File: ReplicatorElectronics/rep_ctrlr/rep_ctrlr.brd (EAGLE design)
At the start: 106.5 x 89 mm, 98 parts, among them IC1 MICROCHIP_PIC32MX7X5F256L-PF, IC2 MICROCHIP_MCP6001-LT, IC3 MICROCHIP_MCP6001-LT, IC4 MICROCHIP_MCP6001-LT, IC5 MICROCHIP_MCP6001-LT, J1 ATX24RH, J10 SBH11-PBPC-D07-ST-BK, J11 SBH11-PBPC-D07-ST-BK, J12 SBH11-PBPC-D07-ST-BK, J13 SBH11-PBPC-D07-ST-BK, J14 SBH11-PBPC-D07-ST-BK, J15 SBH11-PBPC-D07-ST-BK, J16 SBH11-PBPC-D07-ST-BK, J17 SBH11-PBPC-D07-ST-BK, J18 SI-50170-F, J19 70553-0106, J4 RJ11-2L-B, J6 SBH11-PBPC-D05-ST-BK, J7 SBH11-PBPC-D05-ST-BK, J8 SBH11-PBPC-D05-ST-BK, J9 SBH11-PBPC-D05-ST-BK, Q1 ASFL1, Q2 ASFL1, U18 LDS3985XX33

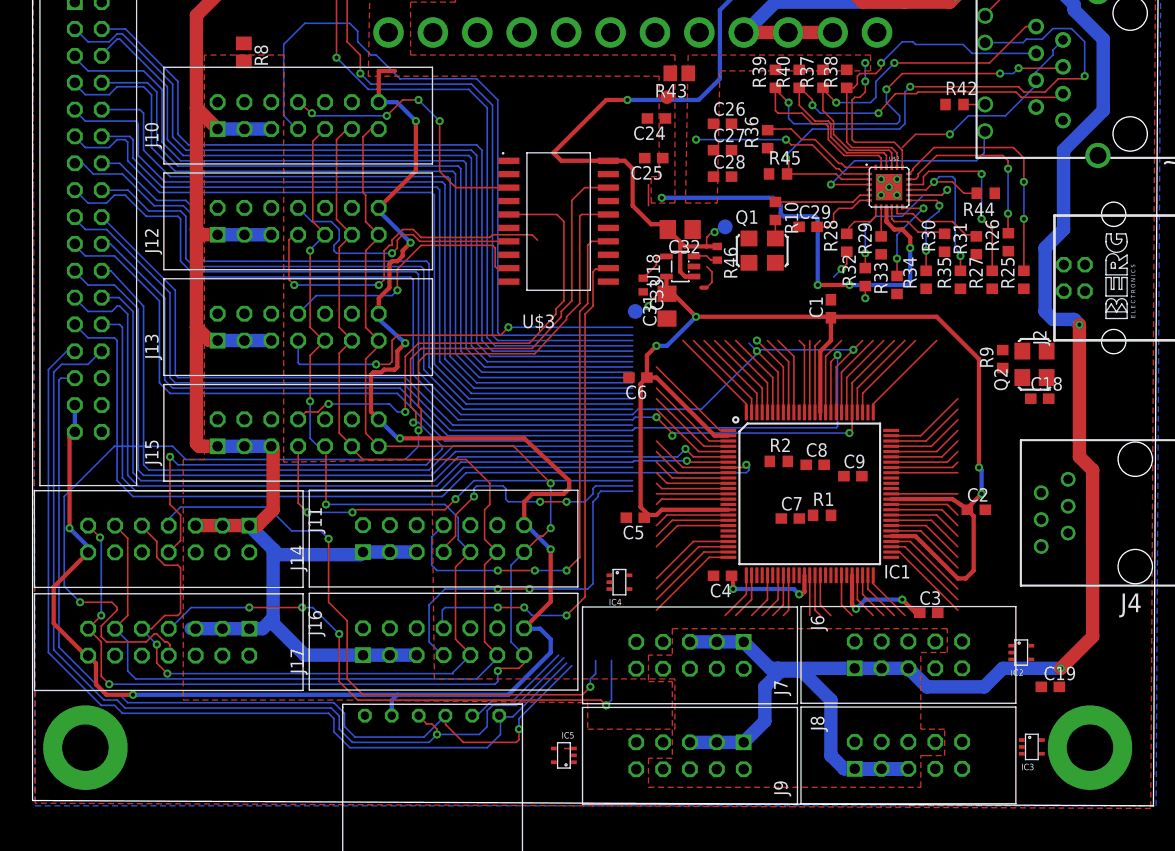
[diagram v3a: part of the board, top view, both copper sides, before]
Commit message: 5/16/12: All but PHY-PIC signals, encoder SPI bus (PIC pins only), servo signals (3.3V side only), and temperature inputs routed.
~ 4 hrs.
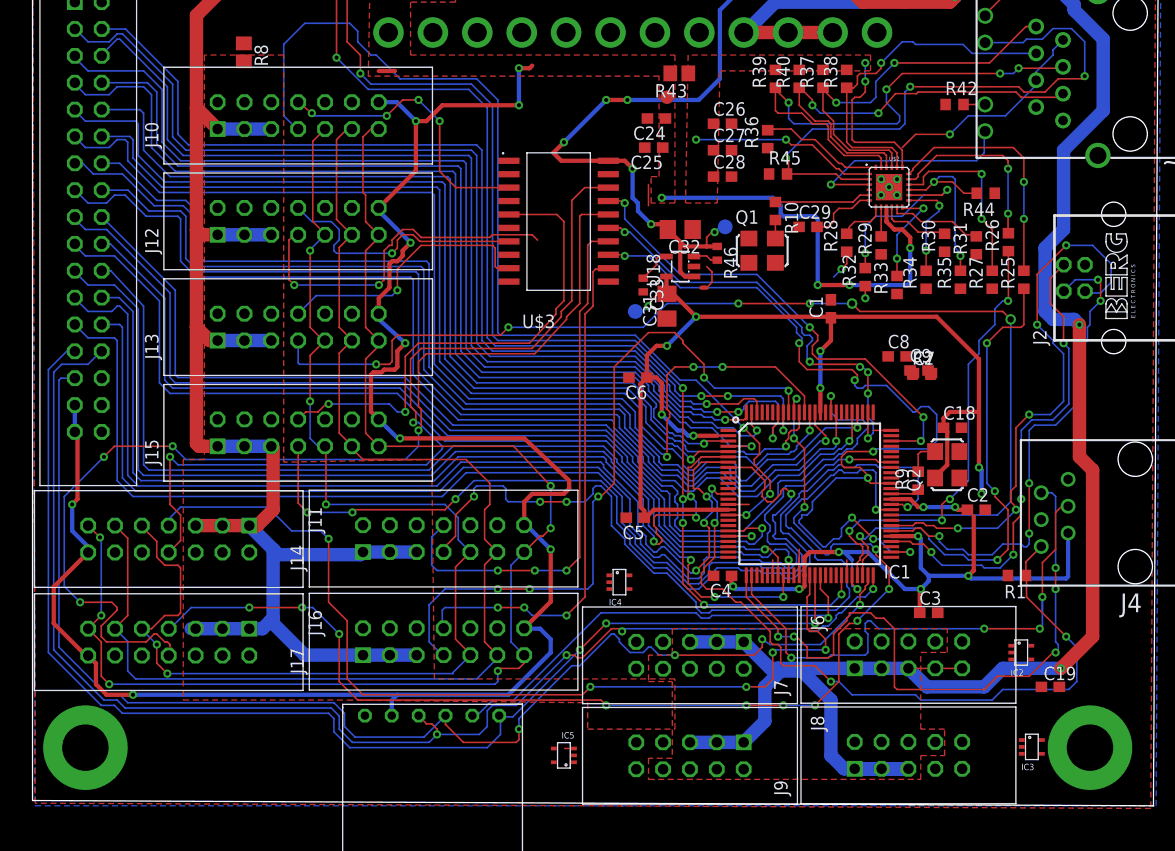
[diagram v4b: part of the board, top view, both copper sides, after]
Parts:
- moved R1 19.3 mm to (93.1, 21.8), turned to 180 degrees
- moved C7 18.6 mm to (84.2, 40.9)
- moved R2 15.8 mm to (84.1, 40.8)
- moved R9 14.0 mm to (83.8, 30.8)
- moved C8 12.9 mm to (81.8, 42.5)
- moved Q2 12.6 mm to (86.5, 32.2)
- moved C9 11.8 mm to (83.8, 41.2)
- moved C18 8.70 mm to (87.0, 35.8)
- moved C25 1.00 mm to (58.8, 62.2)
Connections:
- net DB17: now also U$1.18; no longer U$1.17
- net ENC_3_3V: now also C19.1, Q1.4, R14.2, R15.2, R17.2, R18.2, R20.2, R21.2, R23.2, R24.2
- net VCC: no longer C19.1, Q1.4, R14.2, R15.2, R17.2, R18.2, R20.2, R21.2, R23.2, R24.2
- net X+: now also U$1.17; no longer U$1.18
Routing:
- net SERVO2: track 8.58 -> 82.0 mm, vias 0 -> 8
- net MCLRN: track 6.80 -> 69.2 mm, vias 0 -> 4
- net ENC3_CSN: track 43.6 -> 102.8 mm, vias 2 -> 6
- net PGEC: track 4.63 -> 62.0 mm, vias 0 -> 5
- net ENC6_CSN: track 60.5 -> 110.9 mm, vias 4 -> 13
- net ENC4_CSN: track 31.3 -> 79.9 mm, vias 3 -> 4
- net PGED: track 4.42 -> 51.1 mm, vias 0 -> 4
- net USB_D+: track 7.54 -> 53.1 mm, vias 0 -> 5
- net ENC5_CSN: track 45.3 -> 90.7 mm, vias 3 -> 4
- net ETXD1: track 4.63 -> 48.5 mm, vias 0 -> 4
- net SERVO5: track 0.12 -> 41.6 mm, vias 0 -> 6
- net USB_D-: track 7.75 -> 47.8 mm, vias 0 -> 5
- net A0: track 89.0 -> 128.0 mm, vias 2 -> 7
- net SD_CSN: track 72.7 -> 111.7 mm, vias 0 -> 1
- net SERVO0: track 7.54 -> 46.0 mm, vias 0 -> 4
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
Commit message: 5/19/12: 18 PIC connections left. Ground currently fractured.
~3 hrs spent between last commit and this one.
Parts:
- C10, C11, C12, C13, C14, C15, C16, C17, C18, C7, C8, C9: device resistor:C0603 -> resistor:C0402
- C19, C30: device rcl:C0603 -> resistor:C0402
- R1, R10, R13, R14, R15, R16, R17, R18, R19, R2, R20, R21, R22, R23, R24, R9: device resistor:R0603 -> resistor:R0402
- moved C10 210.2 mm to (88.5, 19.9)
- moved R22 172.2 mm to (48.1, 3.22)
- moved R15 171.7 mm to (93.8, 18.7), turned to 90 degrees
- moved R14 171.4 mm to (95.0, 13.2)
- moved R13 168.7 mm to (94.3, 9.59), turned to 90 degrees
- moved C19 43.9 mm to (53.2, 20.2), turned to 90 degrees
- moved C8 4.83 mm to (86.3, 40.8)
- moved C5 4.81 mm to (54.8, 23.0)
- moved C9 4.26 mm to (86.6, 37.9)
- moved C7 3.20 mm to (86.7, 38.9)
- moved R2 3.01 mm to (86.3, 38.8)
- moved 3.3V 1.52 mm to (57.2, 48.2)
- moved IC4 1.30 mm to (56.1, 20.0), turned to 0 degrees
- moved IC2 1.25 mm to (94.5, 15.2)
- moved Q1 0.50 mm to (69.0, 53.0)
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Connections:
- net A0: now also U$1.24; no longer U$1.1
- net DB1: now also U$1.4; no longer U$1.3
- net DB2: now also U$1.3; no longer U$1.4
- net LCD_WR: now also U$1.1; no longer U$1.24
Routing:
- net ENC2_CSN: track 33.2 -> 166.0 mm, vias 2 -> 16
- net PS_ON: track 2.00 -> 79.1 mm, vias 0 -> 9
- net ERXD0: track 0.00 -> 69.9 mm, vias 0 -> 8
- net ERXD1: track 2.92 -> 72.5 mm, vias 1 -> 8
- net NRST: track 0.00 -> 59.6 mm, vias 0 -> 4
- net ECRSDV: track 0.00 -> 52.3 mm, vias 0 -> 2
- net SERVO7: track 0.00 -> 49.0 mm, vias 0 -> 4
- net EREFCLK: track 1.15 -> 49.7 mm, vias 1 -> 6
- net ERXERR: track 0.00 -> 48.0 mm, vias 0 -> 6
- net A0: track 128.0 -> 99.8 mm, vias 7 -> 5
- net ETXEN: track 0.00 -> 25.3 mm, vias 0 -> 2
- net EMDC: track 0.00 -> 24.7 mm, vias 0 -> 6
- net ETXD0: track 42.7 -> 66.8 mm, vias 4 -> 10
- net EMDIO: track 0.00 -> 24.0 mm, vias 0 -> 4
- net +3V3: track 169.5 -> 191.0 mm, vias 18 -> 27
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
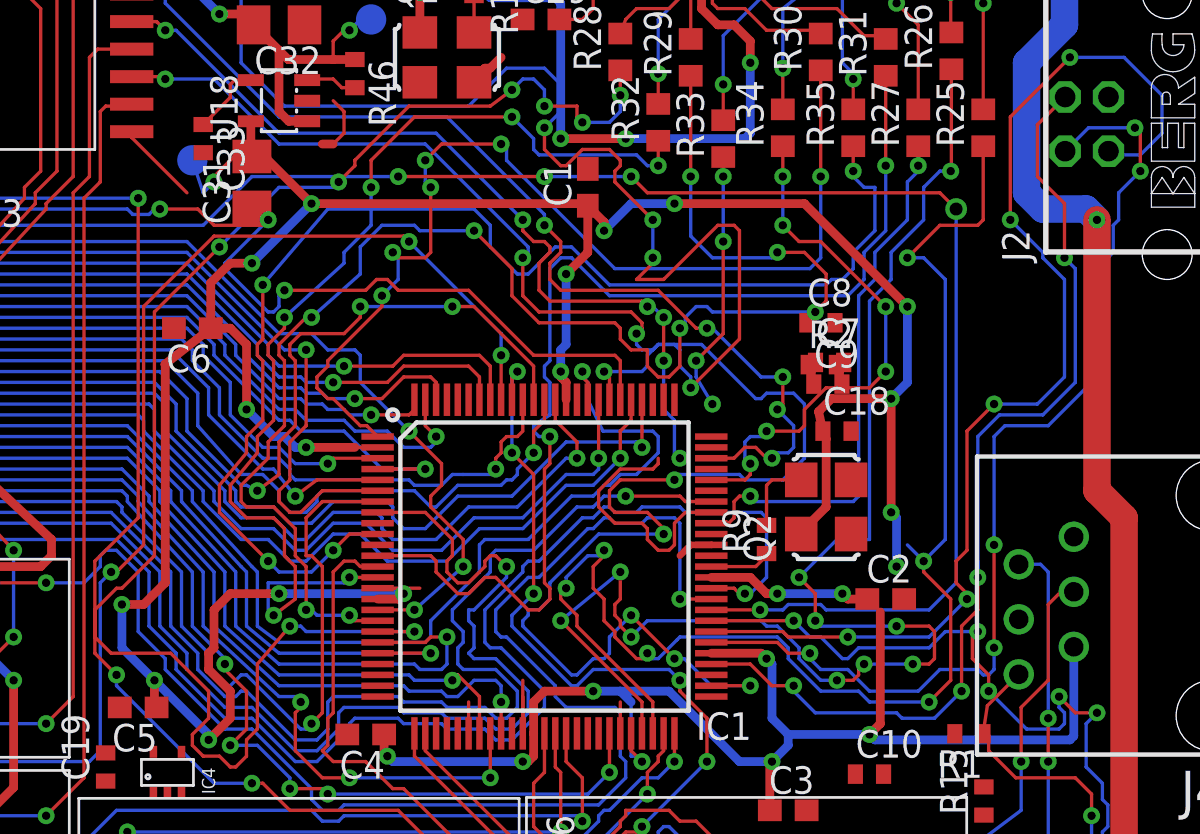
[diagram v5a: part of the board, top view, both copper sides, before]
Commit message: 5/21/12: Fixed GND plane. Still 18 PIC connections remaining...
~ 1 hr.
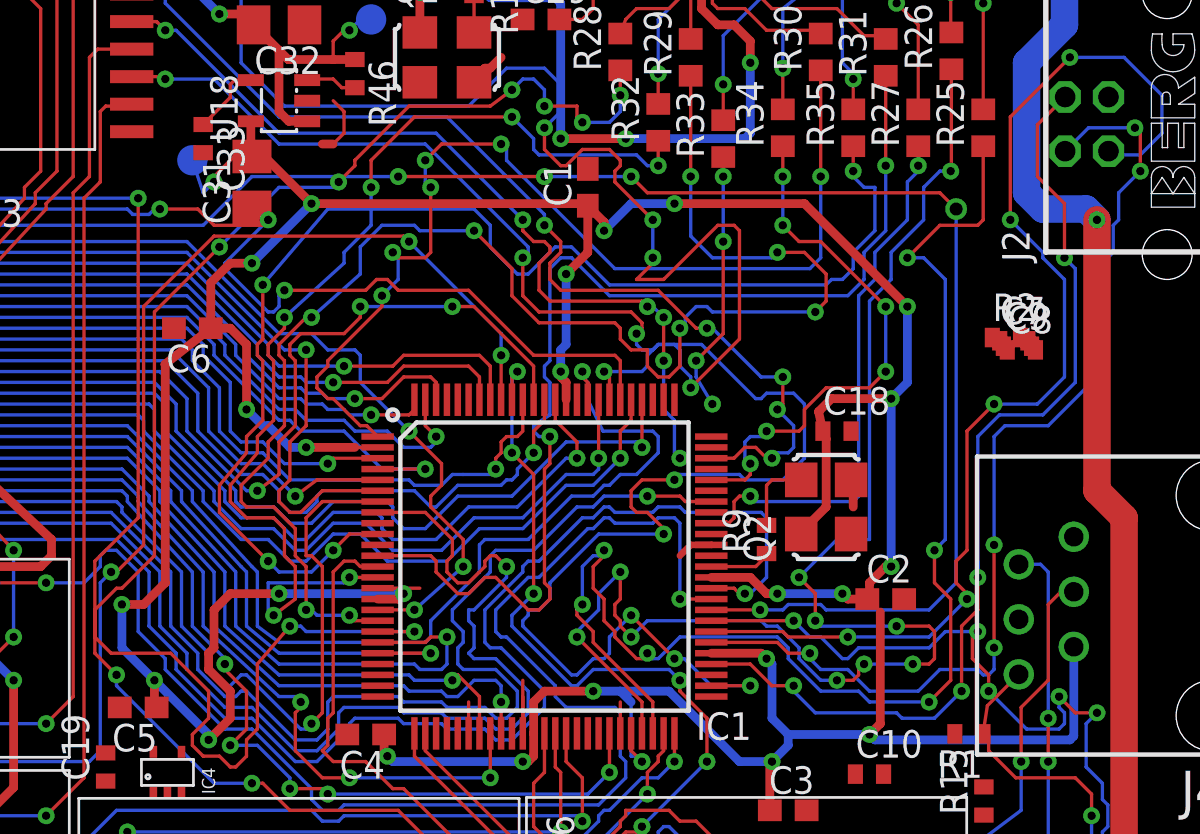
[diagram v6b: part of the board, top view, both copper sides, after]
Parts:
- moved C8 9.33 mm to (95.5, 39.5)
- moved C9 8.92 mm to (95.3, 39.7)
- moved R2 8.59 mm to (94.8, 40.1)
- moved C7 8.56 mm to (95.2, 39.9)
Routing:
- net EMDIO: track 24.0 -> 12.1 mm
- net SERVO3: track 3.88 -> 0.00 mm
- net ETXD1: track 64.7 -> 62.5 mm
- net SERVO2: track 81.7 -> 79.7 mm
- net +3V3: track 191.0 -> 193.0 mm, vias 27 -> 26
- net DGND: track 16.4 -> 17.7 mm
- net ETXD0: track 66.8 -> 66.0 mm

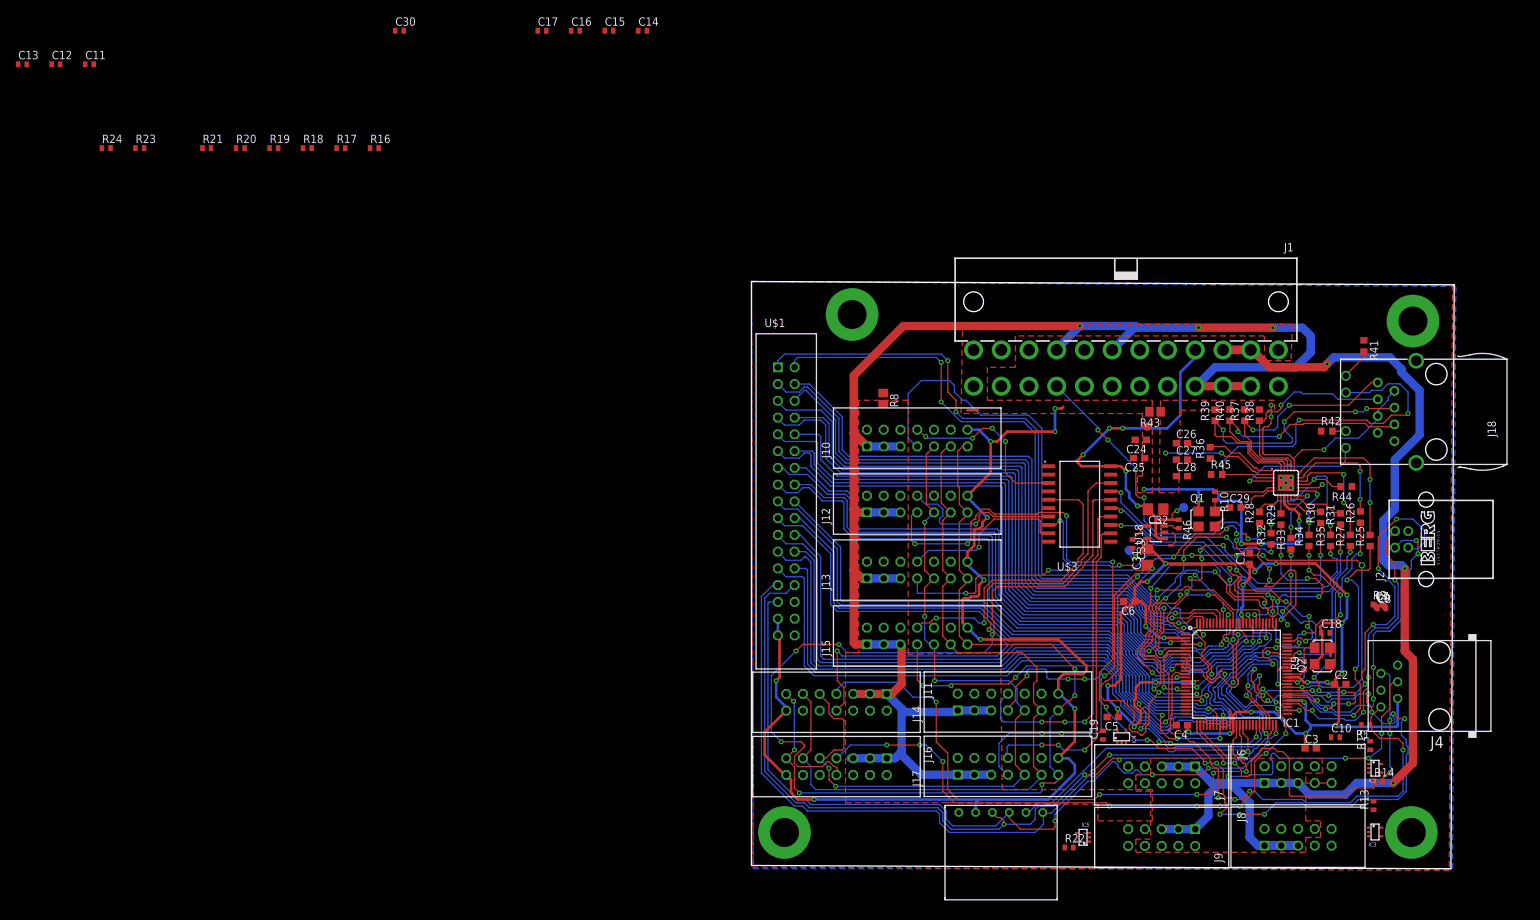
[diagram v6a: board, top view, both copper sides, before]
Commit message: 5/27/12: 5 PIC pins remain to be routed (3 encoder signals and encoder SPI MISO/MOSI), as well as buffers/passives around heater connectors. Cleanup will be required.
~ 6 hrs.
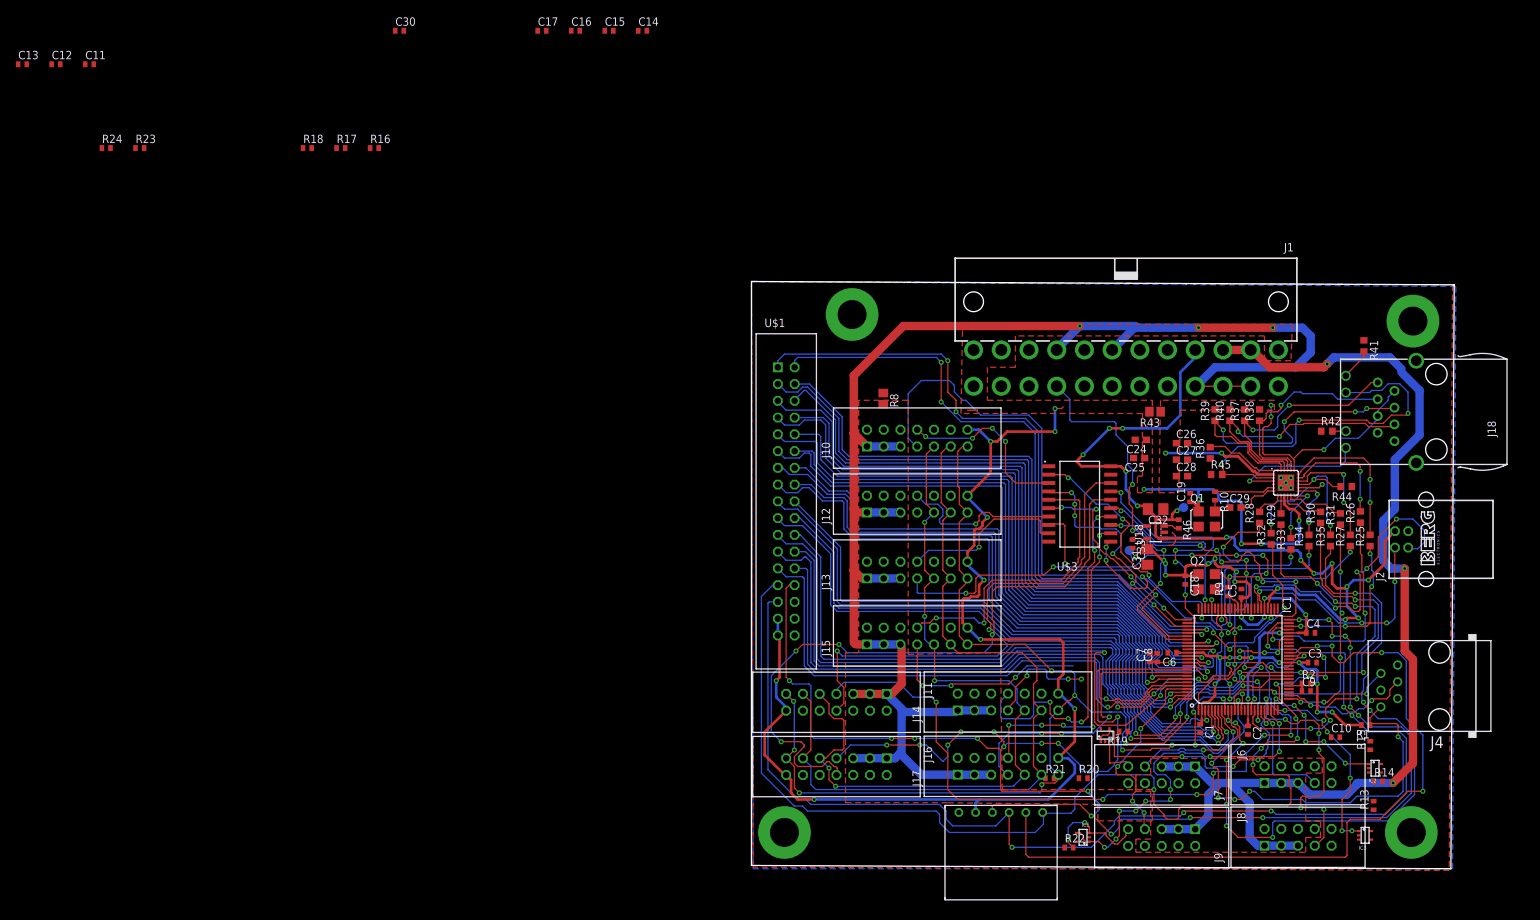
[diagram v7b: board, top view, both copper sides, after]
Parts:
- C1, C2, C3, C4, C5, C6: device resistor:C0603 -> resistor:C0402
- moved R20 159.5 mm to (50.3, 13.7)
- moved R21 159.5 mm to (45.2, 13.7)
- moved R19 156.2 mm to (56.4, 20.8), turned to 180 degrees
- moved C19 38.4 mm to (66.5, 56.2)
- moved C7 35.7 mm to (60.4, 32.0), turned to 90 degrees
- moved C8 34.8 mm to (61.5, 32.0), turned to 90 degrees
- moved C5 27.1 mm to (74.2, 41.8), turned to 90 degrees
- moved C1 26.8 mm to (68.0, 21.2), turned to 270 degrees
- moved C4 24.0 mm to (84.8, 35.8), turned to 0 degrees
- moved C18 22.7 mm to (65.8, 43.8), turned to 270 degrees
- moved Q2 20.8 mm to (69.0, 43.5), turned to 0 degrees
- moved C9 17.0 mm to (84.1, 26.9)
- moved R2 16.1 mm to (84.1, 28.1)
- moved R9 16.1 mm to (72.2, 42.0)
- moved C2 15.7 mm to (75.2, 21.0), turned to 270 degrees
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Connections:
- net A0: now also U$1.23; no longer U$1.24
- net DB0: now also U$1.10; no longer U$1.2
- net DB1: now also U$1.9; no longer U$1.4
- net DB10: now also U$1.7; no longer U$1.10
- net DB11: now also U$1.8; no longer U$1.11
- net DB12: now also U$1.5; no longer U$1.12
- net DB13: now also U$1.6; no longer U$1.13
- net DB14: now also U$1.1; no longer U$1.14
- net DB15: now also U$1.2; no longer U$1.15
- net DB16: now also U$1.4; no longer U$1.16
- net DB17: now also U$1.3; no longer U$1.18
- net DB2: now also U$1.12; no longer U$1.3
- net DB3: now also U$1.11; no longer U$1.5
- net DB4: now also U$1.14; no longer U$1.6
- net DB5: now also U$1.13; no longer U$1.7
- net DB6: now also U$1.16; no longer U$1.8
- net DB7: now also U$1.15; no longer U$1.9
- net HEAT1_ON: now also IC1.21; no longer IC1.96
- net HEAT3_ON: now also IC1.20; no longer IC1.95
- net LCD_CS: now also U$1.19; no longer U$1.22
- net LCD_RD: now also U$1.17; no longer U$1.23
- net LCD_RST: now also U$1.20; no longer U$1.25
- net LCD_WR: now also U$1.18; no longer U$1.1
- net SD_CSN: now also U$1.24; no longer U$1.26
- net TEMP0_BUF: now also IC1.22; no longer IC1.25
- net TEMP3_BUF: now also IC1.25; no longer IC1.22
- net X+: now also IC1.95, U$1.26; no longer IC1.21, U$1.17
- net X-: now also U$1.21; no longer U$1.19
- net Y+: now also IC1.96, U$1.25; no longer IC1.20, U$1.20
- net Y-: now also U$1.22; no longer U$1.21
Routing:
- net ENC2_CSN: track 166.0 -> 0.00 mm, vias 16 -> 0
- net SP_CSN: track 42.5 -> 115.8 mm, vias 1 -> 4
- net SD_SP_MOSI: track 125.2 -> 194.7 mm, vias 4 -> 16
- net +3V3: track 193.0 -> 127.4 mm, vias 26 -> 23
- net ENC4_CSN: track 79.9 -> 16.8 mm, vias 4 -> 3
- net SD_SP_MISO: track 121.1 -> 183.7 mm, vias 4 -> 6
- net ENC5_CSN: track 90.7 -> 30.6 mm, vias 4 -> 3
- net SD_SP_SCK: track 117.8 -> 174.4 mm, vias 3 -> 9
- net TEMP2_BUF: track 0.00 -> 55.1 mm, vias 0 -> 10
- net PGEC: track 61.4 -> 16.5 mm, vias 5 -> 3
- net NRST: track 59.6 -> 104.3 mm, vias 4 -> 10
- net TEMP0_BUF: track 0.00 -> 43.9 mm, vias 0 -> 4
- net SERVO1: track 0.00 -> 39.7 mm, vias 0 -> 4
- net SERVO3: track 0.00 -> 39.5 mm, vias 0 -> 6
- net ENC_MISO: track 128.3 -> 166.8 mm, vias 6 -> 11
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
